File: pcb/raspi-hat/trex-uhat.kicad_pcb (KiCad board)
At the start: 2 copper layers, 89.5 x 30 mm, 23 parts, among them J1 Conn_01x08_Female, J10 RAIL2, J2 RPi_GPIO, J3 Conn_01x03_Female, J4 DFPLAYER_MINI, J5 RAIL1, J6 Conn_01x04_Female, J7 AudioJack3, J8 Jack-DC, J9 Conn_01x05_Female

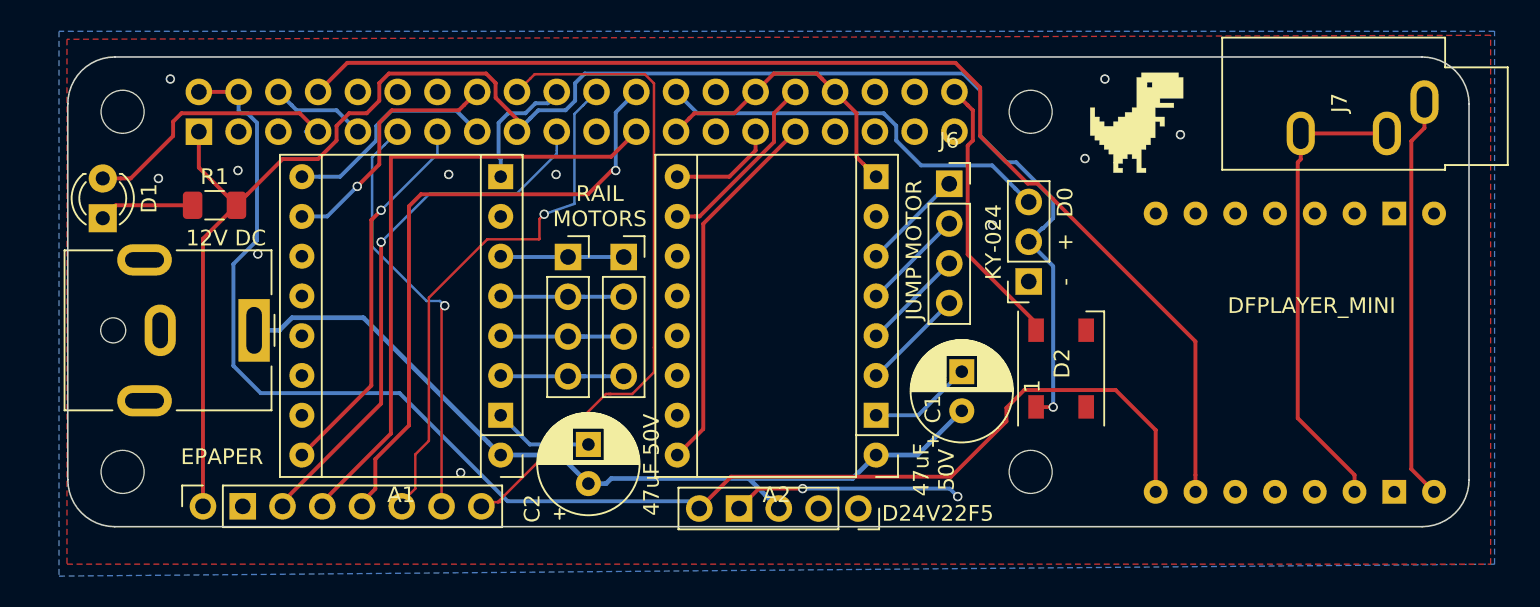
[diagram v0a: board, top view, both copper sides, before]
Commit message: fix(pcb): mirror DRV8880 breakout
We want the potentiometer to be up
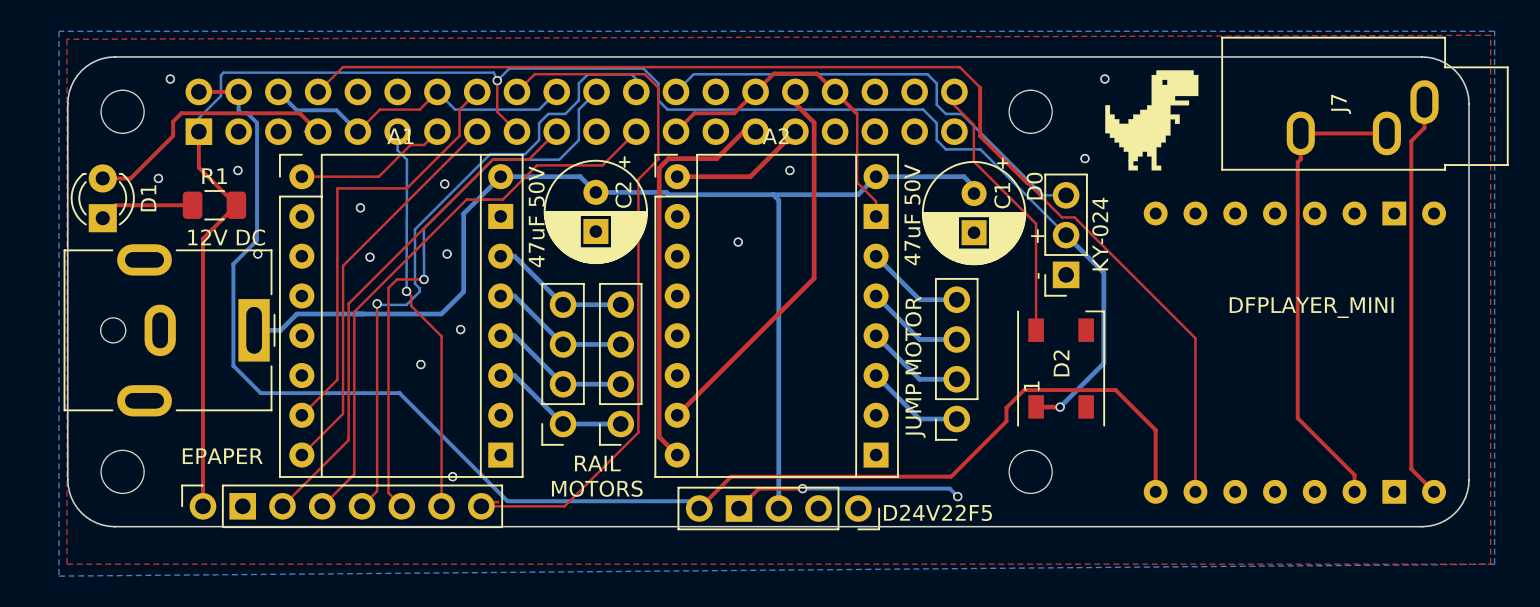
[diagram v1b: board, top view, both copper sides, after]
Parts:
- moved A1 21.8 mm to (27.4, 32.1), turned to 0 degrees
- moved A2 21.8 mm to (51.4, 32.1), turned to 0 degrees
- moved C2 18.6 mm to (46.2, 33.1), turned to 270 degrees
- moved J6 15.0 mm to (69.3, 47.6), turned to 180 degrees
- moved C1 13.9 mm to (70.4, 33.2), turned to 270 degrees
- moved J5 10.7 mm to (44.1, 47.9), turned to 180 degrees
- moved J10 10.7 mm to (47.8, 47.9), turned to 180 degrees
- moved J3 2.43 mm to (76.3, 38.4)
- moved TREX1 0.98 mm to (81.7, 28.5)
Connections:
- A1 pad 1: +12V -> /STP1_EN
- A1 pad 10: /STP1_STEP -> Net-(A1-Pad10)
- A1 pad 15: Net-(A1-Pad15) -> GND
- A1 pad 16: /STP1_EN -> +12V
- A1 pad 2: GND -> Net-(A1-Pad2)
- A1 pad 7: Net-(A1-Pad7) -> /STP1_STEP
- A1 pad 8: GND -> /STP1_DIR
- A1 pad 9: /STP1_DIR -> GND
- A2 pad 1: +12V -> /STP2_EN
- A2 pad 10: /STP2_STEP -> Net-(A2-Pad10)
- A2 pad 15: Net-(A2-Pad15) -> GND
- A2 pad 16: /STP2_EN -> +12V
- A2 pad 2: GND -> Net-(A2-Pad2)
- A2 pad 7: Net-(A2-Pad7) -> /STP2_STEP
- A2 pad 8: GND -> /STP2_DIR
- A2 pad 9: /STP2_DIR -> GND
- J10 pad 1: Net-(A1-Pad6) -> Net-(A1-Pad11)
- J10 pad 2: Net-(A1-Pad5) -> Net-(A1-Pad12)
- J10 pad 3: Net-(A1-Pad4) -> Net-(A1-Pad13)
- J10 pad 4: Net-(A1-Pad3) -> Net-(A1-Pad14)
- J5 pad 1: Net-(A1-Pad6) -> Net-(A1-Pad11)
- J5 pad 2: Net-(A1-Pad5) -> Net-(A1-Pad12)
- J5 pad 3: Net-(A1-Pad4) -> Net-(A1-Pad13)
- J5 pad 4: Net-(A1-Pad3) -> Net-(A1-Pad14)
- J6 pad 1: Net-(A2-Pad6) -> Net-(A2-Pad11)
- J6 pad 2: Net-(A2-Pad5) -> Net-(A2-Pad12)
- J6 pad 3: Net-(A2-Pad4) -> Net-(A2-Pad13)
- J6 pad 4: Net-(A2-Pad3) -> Net-(A2-Pad14)
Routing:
- net +12V: track 54.2 -> 75.2 mm
- net /STP2_DIR: track 6.90 -> 25.9 mm
- net /STP2_EN: track 23.8 -> 8.74 mm
- net /STP1_EN: track 24.2 -> 9.85 mm, vias 1 -> 0
- net /STP2_STEP: track 11.9 -> 24.8 mm
- net /STP1_STEP: track 16.0 -> 27.9 mm, vias 1 -> 0
- net /STP1_DIR: track 14.0 -> 25.3 mm
- net Net-(A1-Pad11): track 0.00 -> 9.02 mm
- net Net-(A1-Pad12): track 0.00 -> 9.02 mm
- net Net-(A1-Pad14): track 0.00 -> 9.02 mm
- net Net-(A1-Pad13): track 0.00 -> 9.02 mm
- net Net-(A1-Pad3): track 8.95 -> 0.00 mm
- net Net-(A1-Pad6): track 8.95 -> 0.00 mm
- net Net-(A1-Pad5): track 8.95 -> 0.00 mm
- net Net-(A1-Pad4): track 8.95 -> 0.00 mm
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
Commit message: fix(pcb): motor connections, replace audio + power jacks
- Change power jack from PJ-063AH to the smaller PJ-102AH
- Change audio jack from SJ1-3533NG to PJ320E
- Fix motor connections: connect Pi to ~SLP instead of EN
- Improve DFPlayer Mini Footprint
- Add silk-screen texts
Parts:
- J7: footprint Connector_Audio:Jack_3.5mm_CUI_SJ1-3533NG_Horizontal -> Connector_Audio:Jack_3.5mm_PJ320E_Horizontal
- J8: footprint Connector_BarrelJack:BarrelJack_CUI_PJ-063AH_Horizontal -> Connector_BarrelJack:BarrelJack_CUI_PJ-102AH_Horizontal
- moved J7 9.43 mm to (89.9, 25.7)
- moved J4 1.85 mm to (80.2, 44.0)
- moved D1 1.25 mm to (15.9, 32.8)
- moved J8 0.65 mm to (24.0, 42.5)
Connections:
- A1 pad 1: /STP1_EN -> Net-(A1-Pad1)
- A1 pad 6: Net-(A1-Pad6) -> /STP1_~SLP
- A2 pad 1: /STP2_EN -> Net-(A2-Pad1)
- A2 pad 6: Net-(A2-Pad6) -> /STP2_~SLP
- J2 pad 13: /STP1_EN -> /STP1_~SLP
- J2 pad 31: /STP2_EN -> /STP2_~SLP
- J7 pad S: Net-(J4-Pad8) -> Net-(J4-Pad6)
- J7 pad T: Net-(J4-Pad6) -> Net-(J4-Pad8)
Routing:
- net /STP1_~SLP: track 0.00 -> 21.1 mm
- net /STP2_~SLP: track 0.00 -> 18.7 mm
- net /STP1_EN: track 9.85 -> 0.00 mm
- net /STP2_EN: track 8.74 -> 0.00 mm
- net Net-(J4-Pad8): track 25.8 -> 33.3 mm
- net Net-(J4-Pad6): track 30.0 -> 35.8 mm
- net +5V: track 92.7 -> 96.5 mm
- net +3V3: track 108.6 -> 111.8 mm
- net Net-(D1-Pad2): track 6.08 -> 5.15 mm
- net /STP2_STEP: track 24.8 -> 25.5 mm
- net /STP2_DIR: track 25.9 -> 26.6 mm
- net Net-(D1-Pad1): track 17.3 -> 16.7 mm
- net GND: vias 17 -> 26
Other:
- board text added: "1"
- board text added: "12V"
- board text added: "5V"
- board text added: "DRV8880 Breakout"
- board text added: "PJ-320E"
